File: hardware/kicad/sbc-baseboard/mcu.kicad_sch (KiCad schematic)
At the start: 41 parts, among them J16 SWD, J3 USB-C HID to target, SW201 RESET, U201 MK64FN1M0VLL12, U202 USBLC6-2SC6, Y201 32.768kHz

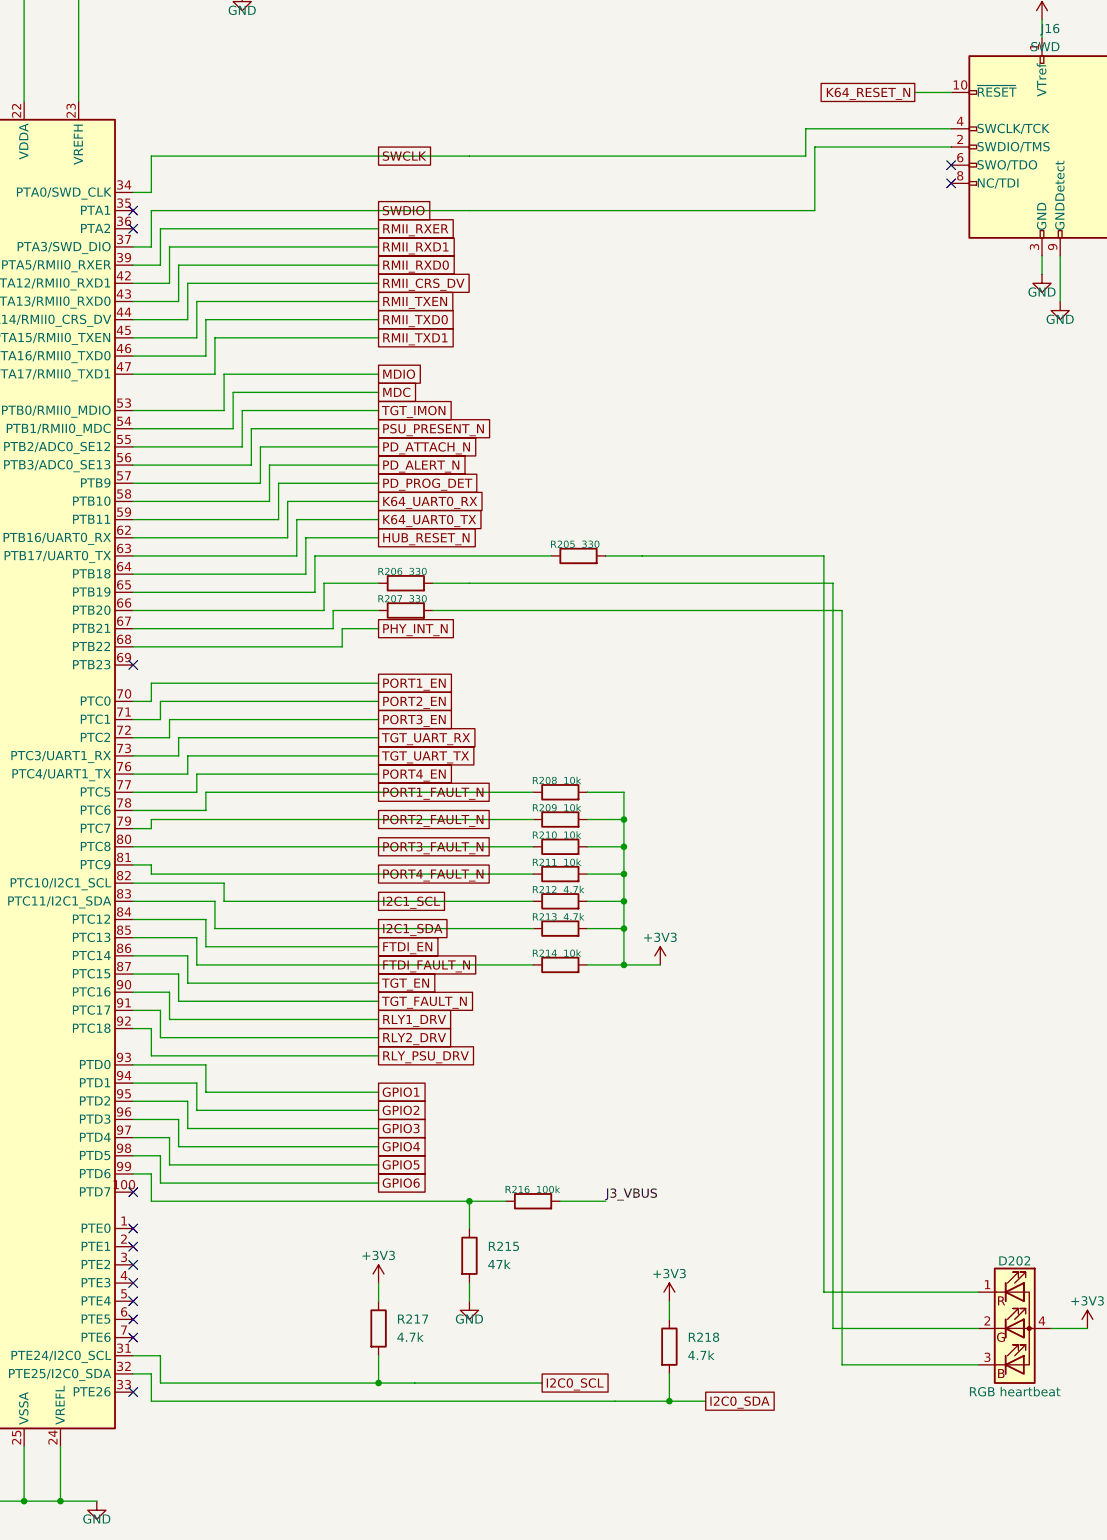
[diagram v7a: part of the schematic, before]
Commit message: The PD inlet and the two 5 V bucks go; a 2.5 mm barrel jack feeds one +5V rail through a reverse-polarity FET
Power in is a 5 V 4 A (20 W) adapter on a Kycon KLDX-0202-BC barrel
jack (J2, centre positive), clamped by an SMAJ5.0A, passed by a
DMP3013SFV P-channel MOSFET (body diode toward the rail, gate at GND,
9.5 mOhm) into +5V: two 47 uF and a 100 nF, an amber LED. The
STUSB4500, its I2C buffer and Qwiic programming header, the two
TPS54560B bucks and their islands, VBUS_IN, +5V_PORTS and +5V_TGT as
separate rails are gone; +5V feeds the port switches, the relays, the
FTDI switch, the 3V3 buck and the TPS26630 eFuse, whose output is the
switched target rail +5V_TGT, now limited to 3 A (RILIM 6.04k, the
datasheet's 18 kOhm.A / IOL). The K64's I2C0 and PD pins are freed.
Classes: PWR_4A (2.5 mm, 1.0 mm vias) for +5V and +5V_TGT in place of
PWR_6A; USB_VBUS_3A keeps the port and FTDI VBUS nets. The directives
anchor the FET behind the jack, drop the bucks' and the PD controller's
templates, and draw the one +5V rail on L4 from the jack to the eFuse.
ERC clean; the placement passes every gate, 481 connections to route.

Co-Authored-By: Claude Fable 5.1 <noreply@anthropic.com>
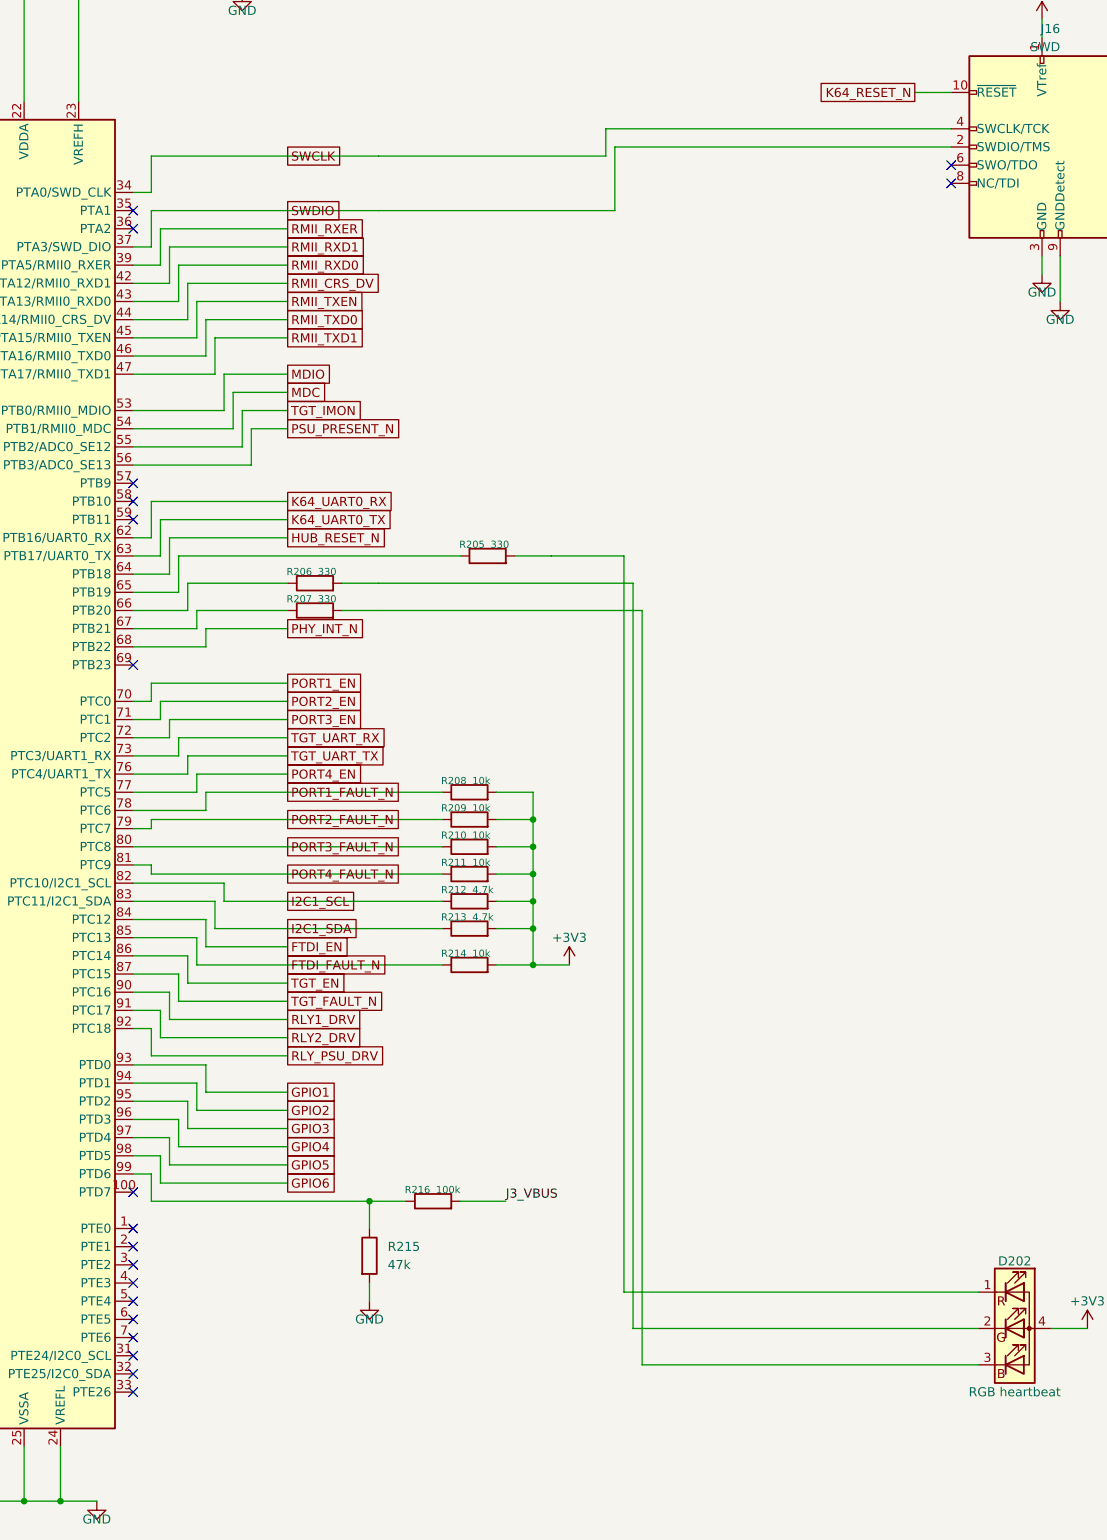
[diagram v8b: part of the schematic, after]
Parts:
- removed R217, R218: 4.7k, Resistor_SMD:R_0603_1608Metric, symbol Device:R
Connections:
- net I2C0_SCL: no longer names the net of U201.31 (PTE24/I2C0_SCL)
- net I2C0_SDA: no longer names the net of U201.32 (PTE25/I2C0_SDA)
- net PD_ALERT_N: no longer names the net of U201.58 (PTB10)
- net PD_ATTACH_N: no longer names the net of U201.57 (PTB9)
- net PD_PROG_DET: no longer names the net of U201.59 (PTB11)
- no-connect marks 28 -> 33
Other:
- moved on the sheet: R205, R206, R207, R208, R209, R210, R211, R212, R213, R214, R215, R216
